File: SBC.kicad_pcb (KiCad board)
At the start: 6 copper layers, 85 x 54 mm, 321 parts, among them J1 USB_OTG, J2 DIN41612_02x10_AB, J3 USB_OTG, J4 Conn_02x20_Counter_Clockwise, J5 Conn_01x15_Socket, J6 Conn_01x06_Socket, U1 STPMIC1APQR, U2 IS43TR16640C-125JBL, U3 ECMF02-2AMX6, U4 ECMF02-2AMX6, U5 STM32MP157FADx, U6 IS21ES08GA-JQLI-TR, U7 LAN8720A, U8 ARJM11C7-114-BA-EW2, X1 ASE-24MHz, Y1 25MHz

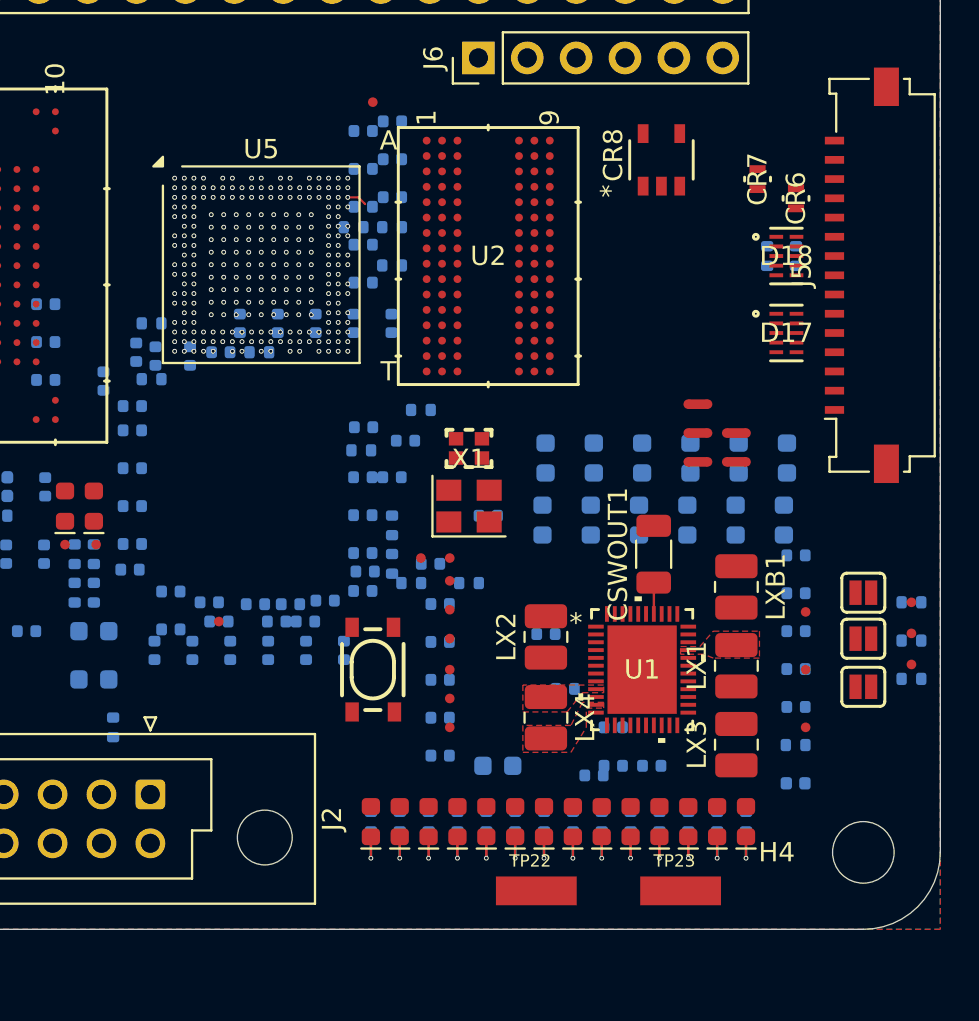
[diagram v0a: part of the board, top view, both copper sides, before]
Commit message: Routed PMIC and started on MPU
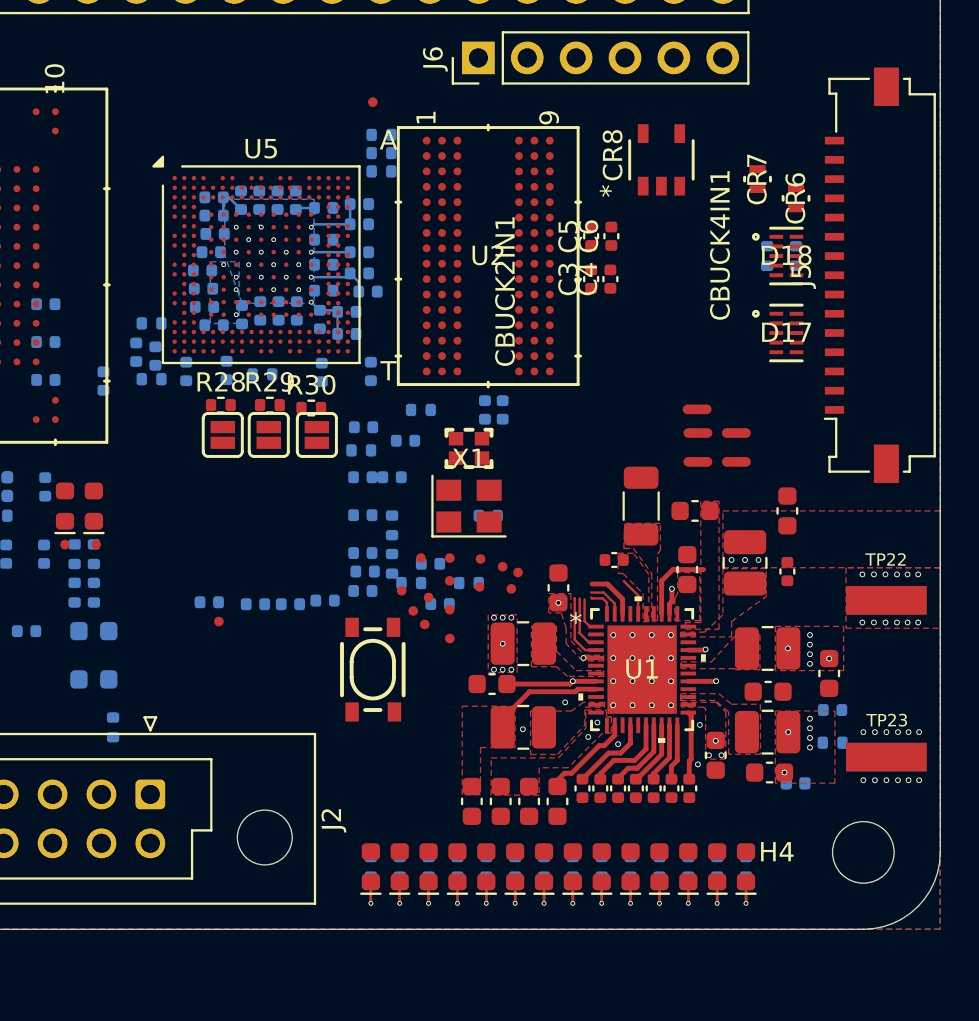
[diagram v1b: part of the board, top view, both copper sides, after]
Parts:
- C3, C4, C5, C6, CBSTOUT1, CBUCK1IN1, CBUCK2IN1, CBUCK3IN1, CBUCK4IN1, CLDO16IN1, CLDO1OUT1, CLDO25IN1, CLDO2OUT1, CLDO3IN1, CLDO3OUT1, CLDO4OUT1, CLDO5OUT1, CLDO6OUT1, CVBUSOTG1, CVIN1, CVLXBST1, CVOUT1, CVOUT2, CVOUT3, CVOUT4, CVREF1, R28, R29, R30: moved to F.Cu
- moved R28 37.3 mm to (77.6, 66.8), turned to 0 degrees
- moved R29 35.5 mm to (80.2, 66.8), turned to 0 degrees
- moved JP1 34.3 mm to (77.7, 68.3), turned to 90 degrees
- moved R30 34.2 mm to (82.3, 66.9), turned to 0 degrees
- moved JP2 32.7 mm to (80.1, 68.3), turned to 90 degrees
- moved JP3 31.3 mm to (82.6, 68.3), turned to 90 degrees
- moved C16 26.0 mm to (81.5, 56.1), turned to 90 degrees
- moved C15 25.5 mm to (80.5, 56.1), turned to 90 degrees
- moved C6 24.5 mm to (97.9, 58.0), turned to 90 degrees
- moved TP22 23.6 mm to (112.2, 76.9)
- moved C5 23.1 mm to (96.8, 58.0), turned to 90 degrees
- moved TP19 23.1 mm to (91.1, 74.8)
- moved C19 22.8 mm to (77.2, 56.9), turned to 180 degrees
- moved C17 22.7 mm to (77.3, 57.9), turned to 180 degrees
- moved TP18 22.6 mm to (91.0, 76.2)
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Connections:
- NT1 pad 2: /Power/SWIN -> /Power/BSTOUT
- U1 pad 37: /Power/SWIN -> /Power/BSTOUT
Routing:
- net /MPU/VDD_DDR: track 0.00 -> 16.6 mm
- net VIN: track 0.00 -> 12.8 mm, vias 0 -> 22
- net /MPU/VDDCORE: track 0.00 -> 9.01 mm, vias 14 -> 23
- net /Power/VOUT4: track 0.00 -> 6.25 mm, vias 0 -> 7
- net VDD: track 0.00 -> 5.54 mm, vias 8 -> 11
- net /Power/LDO3OUT: track 0.00 -> 4.79 mm
- net /NAND/VDD: track 0.00 -> 4.42 mm
- net /MPU/DDR_VREF: track 0.00 -> 4.21 mm, vias 1 -> 0
- net /Power/BSTOUT: track 0.00 -> 4.15 mm
- net /MPU/VDDA: track 0.00 -> 3.56 mm, vias 2 -> 0
- net /MPU/I2C_SCL: track 0.00 -> 3.47 mm, vias 1 -> 0
- net /Power/LDO5OUT: track 0.00 -> 3.39 mm
- net /Power/LDO6OUT: track 0.00 -> 3.14 mm
- net /MPU/I2C_SDA: track 0.00 -> 2.85 mm, vias 1 -> 0
- net /Power/VIO: track 0.00 -> 2.68 mm
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- added copper zone on F.Cu, net /MPU/VBUS_HOST
- added copper zone on F.Cu, net /MPU/VBUS_OTG
- added copper zone on B.Cu, net /MPU/VDDCORE
- added copper zone on F.Cu, net /MPU/VDDCORE
- added copper zone on In2.Cu, net /MPU/VDDCORE
- added copper zone on F.Cu, net /Power/BSTOUT
- added copper zone on F.Cu, net /Power/LDO4OUT
- added copper zone on F.Cu, net /Power/VLX1
- added copper zone on F.Cu, net /Power/VLX3
- added copper zone on F.Cu, net /Power/VLX4
- added copper zone on F.Cu, net /Power/VLXBST
- added copper zone on F.Cu, net /Power/VOUT4
- added copper zone on B.Cu, net VDD
- added copper zone on F.Cu, net VIN
- added copper zone on In2.Cu, net VIN

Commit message: Routing DDR
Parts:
- moved Y1 9.00 mm to (81.8, 71.3)
- moved X1 8.17 mm to (82.6, 74.1)
- moved CBUCK1IN1 0.50 mm to (92.2, 81.2)
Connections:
- CLDO3IN1 pad 1: VIN -> /Power/LDO3IN
- NT3 pad 2: VIN -> /Power/LDO3IN
- U1 pad 13: VIN -> /Power/LDO3IN
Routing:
- net VDD: track 5.54 -> 9.93 mm
- net /MPU/VDD_DDR: track 16.6 -> 19.2 mm, vias 4 -> 27
- net GND: vias 33 -> 36
- added copper zone on In2.Cu, net /MPU/VDD_DDR
- added copper zone on In2.Cu, net VDD

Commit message: I am not good at routing
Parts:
- moved CR8 25.0 mm to (125.2, 57.3)
- moved C6 19.5 mm to (81.2, 47.9)
- moved C3 19.5 mm to (80.2, 50.1)
- moved C4 19.5 mm to (81.2, 50.1)
- moved C5 19.5 mm to (80.2, 47.9)
- moved R50 5.84 mm to (76.5, 67.8)
- moved C47 4.31 mm to (95.6, 66.7)
- moved C48 4.31 mm to (96.5, 66.7)
- moved U2 3.86 mm to (95.3, 59.7), turned to -90 degrees
- moved C22 3.73 mm to (85.8, 57.0)
- moved C29 3.70 mm to (83.0, 61.9), turned to -90 degrees
- moved C30 3.08 mm to (85.8, 62.8), turned to 0 degrees
- moved C37 2.07 mm to (85.8, 61.8)
- moved C31 1.96 mm to (85.8, 60.9)
- moved C34 1.88 mm to (83.4, 56.1), turned to 90 degrees
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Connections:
- NT1 pad 2: /Power/BSTOUT -> /Power/SWIN
- U1 pad 37: /Power/BSTOUT -> /Power/SWIN
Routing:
- net /A0: track 0.00 -> 13.1 mm, vias 0 -> 2
- net /A4: track 0.00 -> 12.8 mm, vias 0 -> 2
- net /A8: track 0.00 -> 12.8 mm, vias 0 -> 2
- net /A10: track 0.00 -> 11.5 mm, vias 0 -> 2
- net /MPU/VDD_DDR: track 19.2 -> 8.09 mm
- net /A5: track 0.00 -> 10.5 mm, vias 0 -> 2
- net /A3: track 0.00 -> 9.62 mm, vias 0 -> 2
- net /A12: track 0.00 -> 8.85 mm, vias 0 -> 2
- net /A2: track 0.00 -> 8.68 mm, vias 0 -> 2
- net /A6: track 0.00 -> 8.40 mm, vias 0 -> 2
- net /A7: track 0.00 -> 8.18 mm, vias 0 -> 2
- net /A1: track 0.00 -> 7.18 mm, vias 0 -> 2
- net /A9: track 0.00 -> 7.08 mm, vias 0 -> 2
- net /A11: track 0.00 -> 6.75 mm, vias 0 -> 2
- net /Power/SWIN: track 0.00 -> 4.15 mm
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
